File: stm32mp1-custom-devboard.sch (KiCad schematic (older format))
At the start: 0 parts

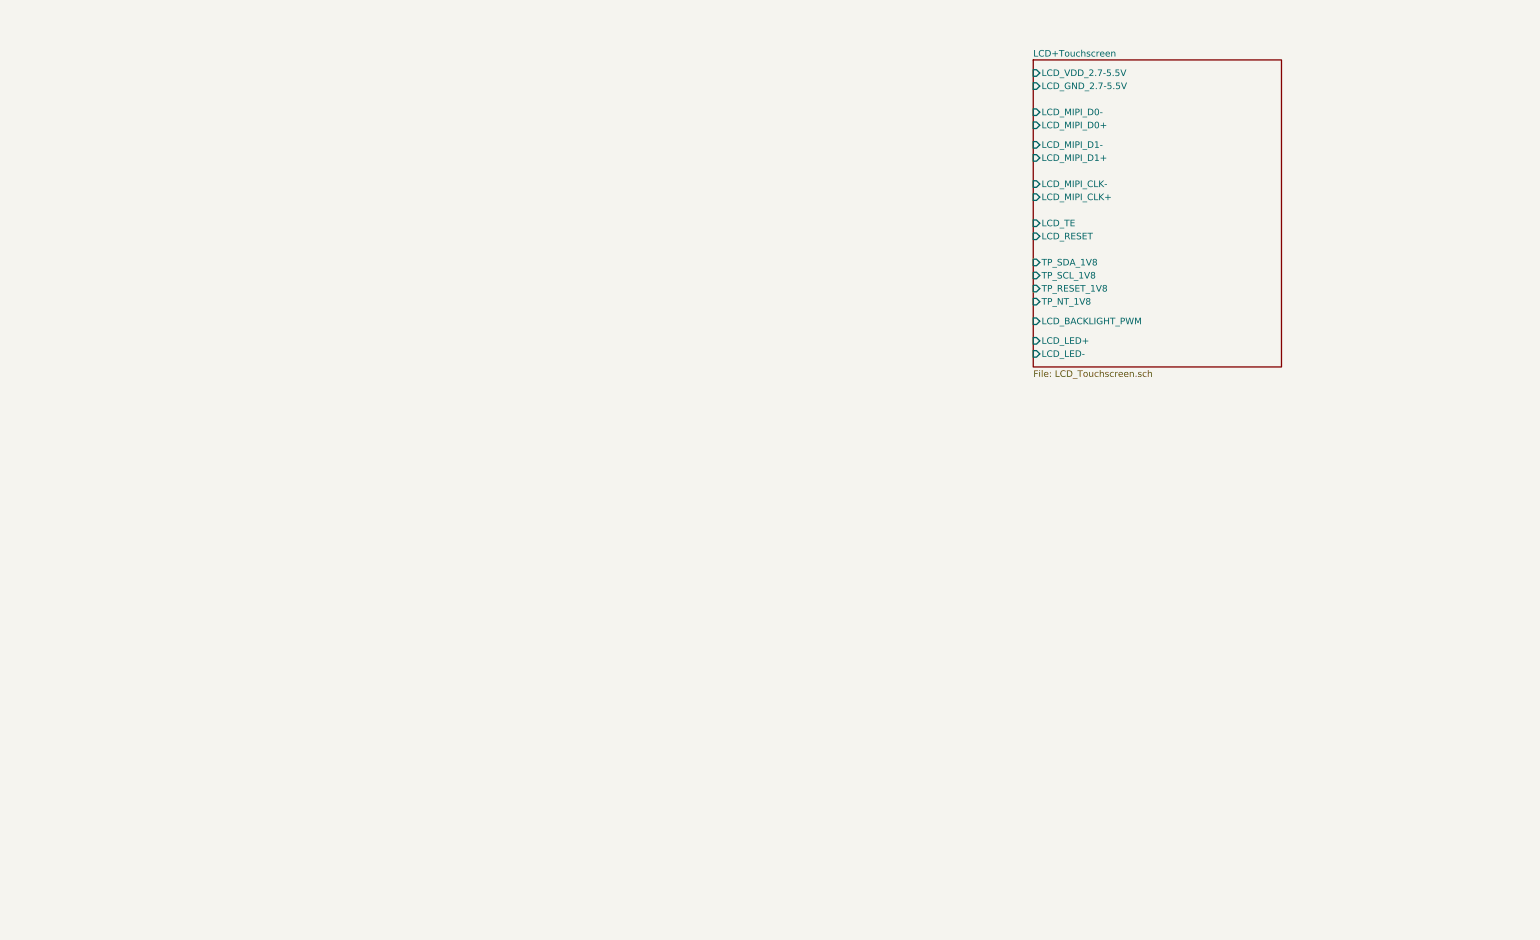
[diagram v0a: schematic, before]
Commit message: Added stm32mp1 module and arduino shield
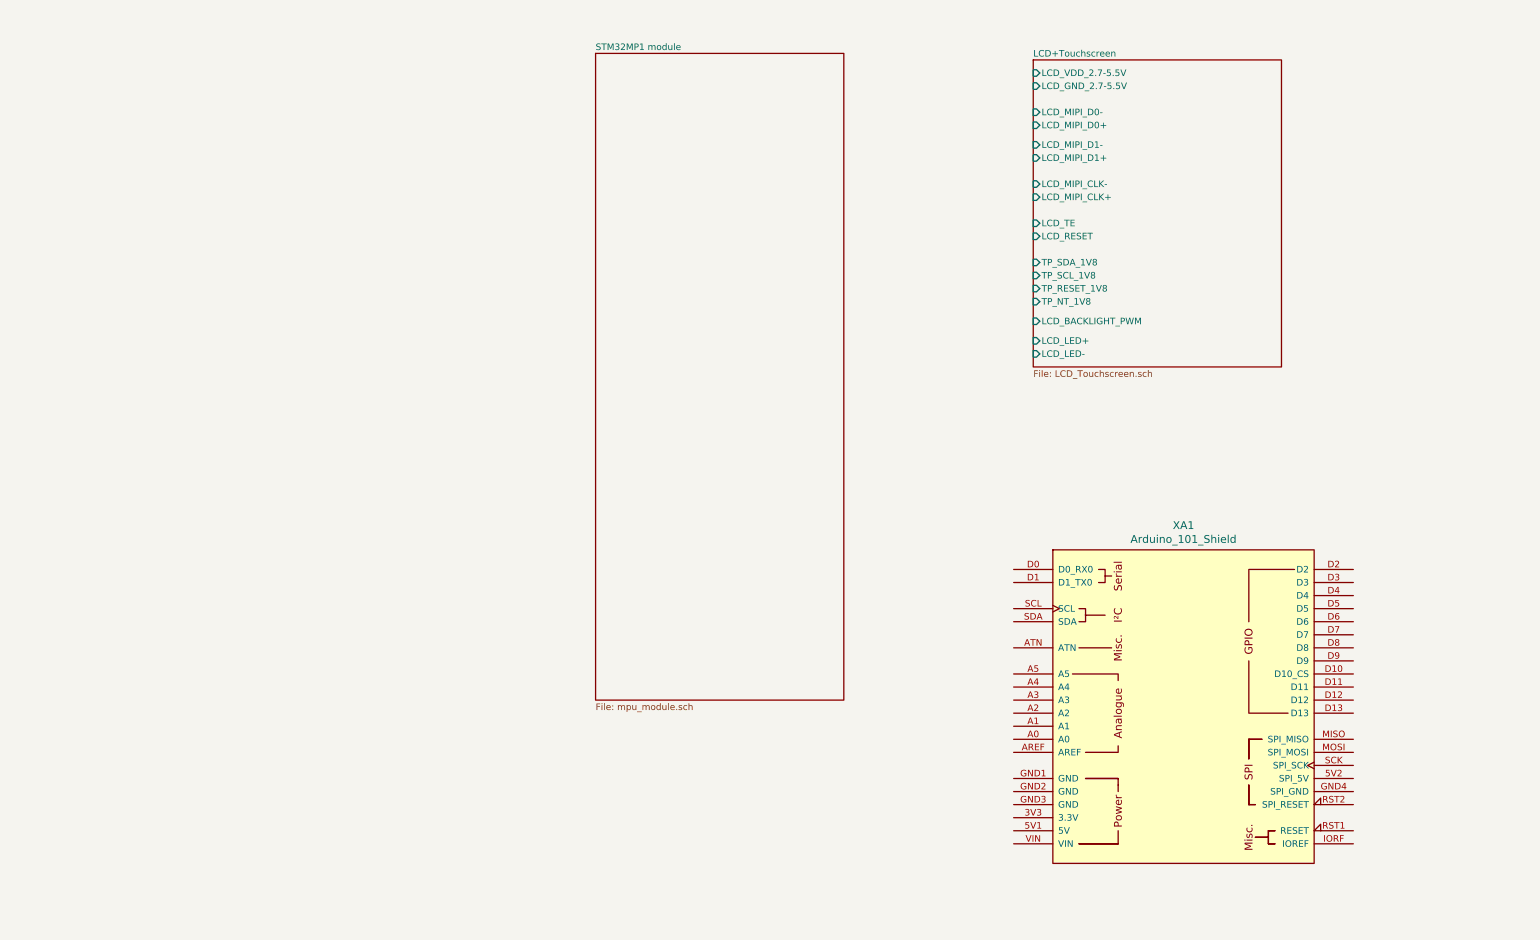
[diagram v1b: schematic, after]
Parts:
- added XA1: Arduino_101_Shield, Arduino:Arduino_101_Shield, symbol arduino:Arduino_101_Shield
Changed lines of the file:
@@
 $Descr A3 16535 11693
 encoding utf-8
-Sheet 1 4
+Sheet 1 5
 Title "stm32mp1-custom-devboard"
 Date "2020-12-19"
@@
 F18 "LCD_LED-" I L 10800 3900 50
 $EndSheet
+$Sheet
+S 7450 1600 1900 4950
+U 5FDE4F7C
+F0 "STM32MP1 module" 50
+F1 "mpu_module.sch" 50
+$EndSheet
+$Comp
+L arduino:Arduino_101_Shield XA1
+U 1 1 5FEBC8FE
+P 11950 6600
+F 0 "XA1" H 11950 7987 60  0000 C CNN
+F 1 "Arduino_101_Shield" H 11950 7881 60  0000 C CNN
+F 2 "Arduino:Arduino_101_Shield" H 13750 10350 60  0001 C CNN
+F 3 "" H 13750 10350 60  0001 C CNN
+	1    11950 6600
+	1    0    0    -1
+$EndComp
 $EndSCHEMATC

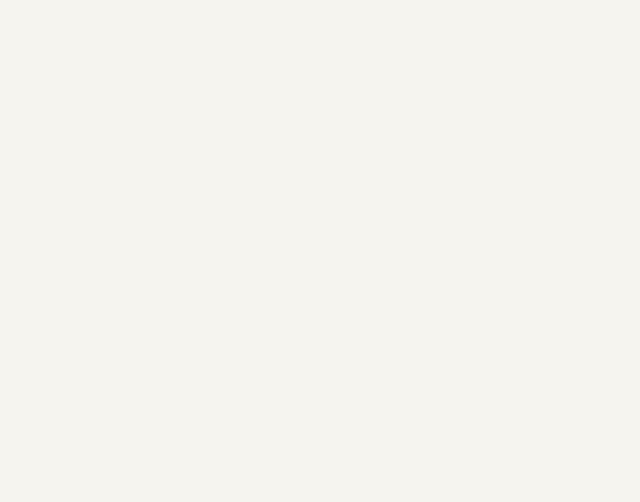
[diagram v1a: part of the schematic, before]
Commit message: Added new components and hierarchical sheets
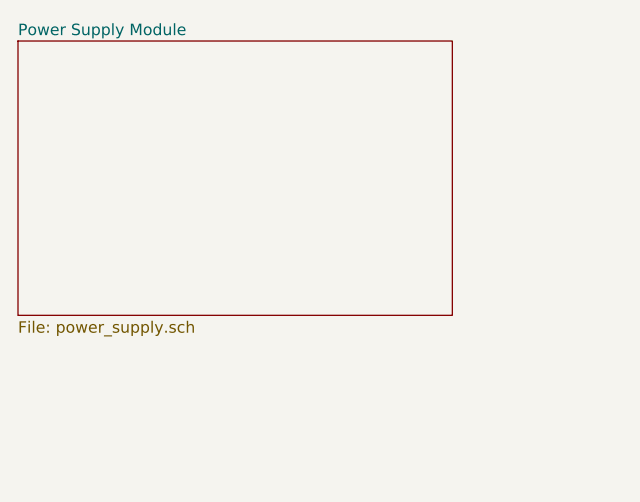
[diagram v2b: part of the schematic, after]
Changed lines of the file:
@@
 $Descr A3 16535 11693
 encoding utf-8
-Sheet 1 5
+Sheet 1 6
 Title "stm32mp1-custom-devboard"
 Date "2020-12-19"
@@
 	1    0    0    -1
 $EndComp
+$Sheet
+S 4400 1600 1900 1200
+U 5FDE84C9
+F0 "Power Supply Module" 50
+F1 "power_supply.sch" 50
+$EndSheet
 $EndSCHEMATC

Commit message: Added power source module
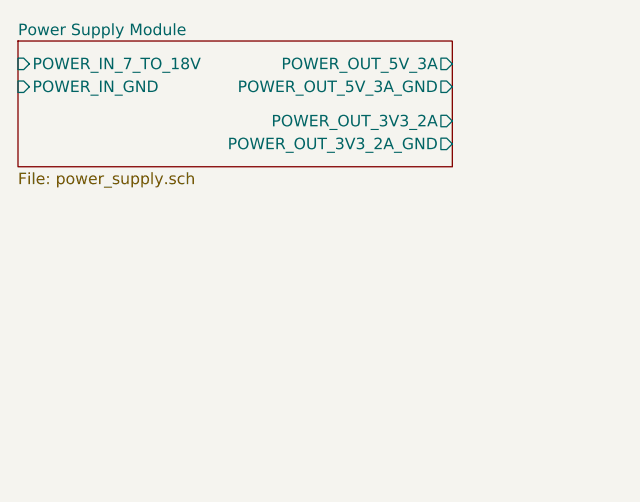
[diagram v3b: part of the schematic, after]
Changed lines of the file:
@@
 $EndComp
 $Sheet
-S 4400 1600 1900 1200
+S 4400 1600 1900 550
 U 5FDE84C9
 F0 "Power Supply Module" 50
 F1 "power_supply.sch" 50
+F2 "POWER_IN_7_TO_18V" I L 4400 1700 50
+F3 "POWER_IN_GND" I L 4400 1800 50
+F4 "POWER_OUT_5V_3A" O R 6300 1700 50
+F5 "POWER_OUT_5V_3A_GND" O R 6300 1800 50
+F6 "POWER_OUT_3V3_2A" O R 6300 1950 50
+F7 "POWER_OUT_3V3_2A_GND" O R 6300 2050 50
 $EndSheet
 $EndSCHEMATC

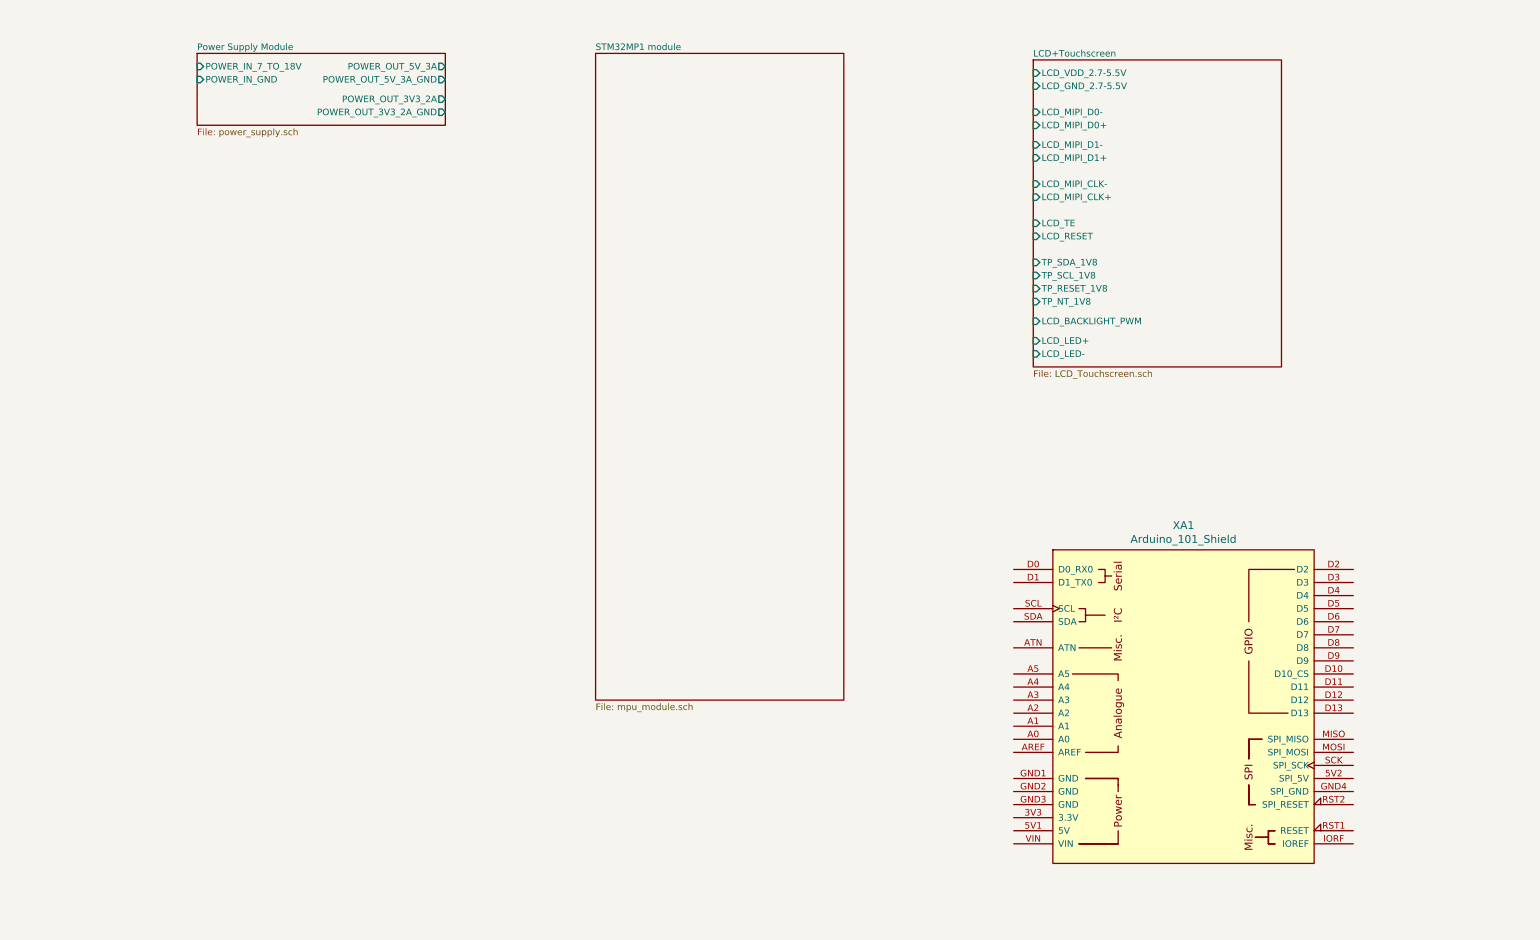
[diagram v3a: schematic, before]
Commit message: Added Mipi Dsi connection, started stlink module
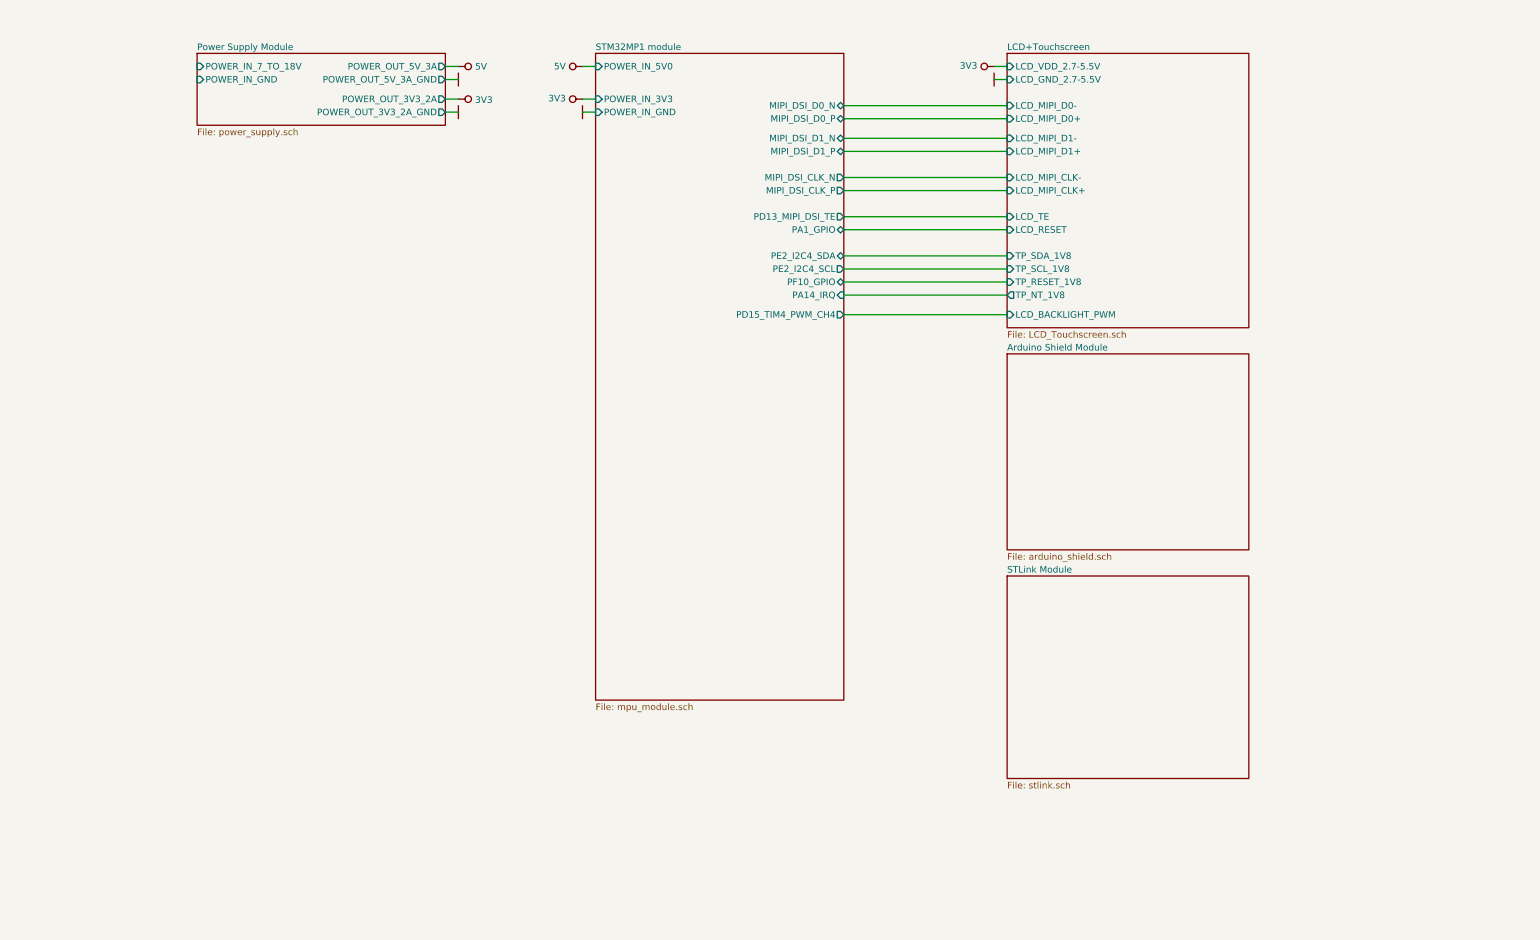
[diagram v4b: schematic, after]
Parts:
- removed XA1: Arduino_101_Shield, Arduino:Arduino_101_Shield, symbol arduino:Arduino_101_Shield
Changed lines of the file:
@@
 $Descr A3 16535 11693
 encoding utf-8
-Sheet 1 6
+Sheet 1 8
 Title "stm32mp1-custom-devboard"
 Date "2020-12-19"
@@
 $EndDescr
 $Sheet
-S 10800 1650 1900 2350
+S 10600 1600 1850 2100
 U 5EA691F1
 F0 "LCD+Touchscreen" 50
 F1 "LCD_Touchscreen.sch" 50
-F2 "LCD_MIPI_D1-" I L 10800 2300 50
-F3 "LCD_MIPI_D1+" I L 10800 2400 50
-F4 "LCD_MIPI_D0-" I L 10800 2050 50
-F5 "LCD_MIPI_D0+" I L 10800 2150 50
-F6 "LCD_MIPI_CLK-" I L 10800 2600 50
-F7 "LCD_MIPI_CLK+" I L 10800 2700 50
-F8 "LCD_BACKLIGHT_PWM" I L 10800 3650 50
-F9 "LCD_VDD_2.7-5.5V" I L 10800 1750 50
-F10 "TP_SDA_1V8" I L 10800 3200 50
-F11 "TP_SCL_1V8" I L 10800 3300 50
-F12 "TP_RESET_1V8" I L 10800 3400 50
-F13 "TP_NT_1V8" I L 10800 3500 50
-F14 "LCD_RESET" I L 10800 3000 50
-F15 "LCD_TE" I L 10800 2900 50
-F16 "LCD_GND_2.7-5.5V" I L 10800 1850 50
-F17 "LCD_LED+" I L 10800 3800 50
-F18 "LCD_LED-" I L 10800 3900 50
+F2 "LCD_MIPI_D1-" I L 10600 2250 50
+F3 "LCD_MIPI_D1+" I L 10600 2350 50
+F4 "LCD_MIPI_D0-" I L 10600 2000 50
+F5 "LCD_MIPI_D0+" I L 10600 2100 50
+F6 "LCD_MIPI_CLK-" I L 10600 2550 50
+F7 "LCD_MIPI_CLK+" I L 10600 2650 50
+F8 "LCD_BACKLIGHT_PWM" I L 10600 3600 50
+F9 "LCD_VDD_2.7-5.5V" I L 10600 1700 50
+F10 "TP_SDA_1V8" I L 10600 3150 50
+F11 "TP_SCL_1V8" I L 10600 3250 50
+F12 "TP_RESET_1V8" I L 10600 3350 50
+F13 "LCD_RESET" I L 10600 2950 50
+F14 "LCD_TE" I L 10600 2850 50
+F15 "LCD_GND_2.7-5.5V" I L 10600 1800 50
+F16 "TP_NT_1V8" O L 10600 3450 50
 $EndSheet
 $Sheet
@@
 F0 "STM32MP1 module" 50
 F1 "mpu_module.sch" 50
-$EndSheet
-$Comp
-L arduino:Arduino_101_Shield XA1
-U 1 1 5FEBC8FE
-P 11950 6600
-F 0 "XA1" H 11950 7987 60  0000 C CNN
-F 1 "Arduino_101_Shield" H 11950 7881 60  0000 C CNN
-F 2 "Arduino:Arduino_101_Shield" H 13750 10350 60  0001 C CNN
-F 3 "" H 13750 10350 60  0001 C CNN
-	1    11950 6600
-	1    0    0    -1
-$EndComp
+F2 "MIPI_DSI_CLK_P" O R 9350 2650 50
+F3 "MIPI_DSI_CLK_N" O R 9350 2550 50
+F4 "MIPI_DSI_D1_P" B R 9350 2350 50
+F5 "MIPI_DSI_D1_N" B R 9350 2250 50
+F6 "MIPI_DSI_D0_P" B R 9350 2100 50
+F7 "MIPI_DSI_D0_N" B R 9350 2000 50
+F8 "POWER_IN_5V0" I L 7450 1700 50
+F9 "POWER_IN_3V3" I L 7450 1950 50
+F10 "POWER_IN_GND" I L 7450 2050 50
+F11 "PE2_I2C4_SCL" O R 9350 3250 50
+F12 "PE2_I2C4_SDA" B R 9350 3150 50
+F13 "PD15_TIM4_PWM_CH4" O R 9350 3600 50
+F14 "PA14_IRQ" I R 9350 3450 50
+F15 "PA1_GPIO" B R 9350 2950 50
+F16 "PF10_GPIO" B R 9350 3350 50
+F17 "PD13_MIPI_DSI_TE" O R 9350 2850 50
+$EndSheet
 $Sheet
 S 4400 1600 1900 550
@@
 F7 "POWER_OUT_3V3_2A_GND" O R 6300 2050 50
 $EndSheet
+$Comp
+L power:5V #PWR0101
+U 1 1 5FDFA2F4
+P 6400 1700
+F 0 "#PWR0101" V 6350 1700 20  0001 C CNN
+F 1 "5V" V 6401 1828 50  0000 L CNN
+F 2 "" H 6400 1700 60  0000 C CNN
+F 3 "" H 6400 1700 60  0000 C CNN
+	1    6400 1700
+	0    1    1    0
+$EndComp
+$Comp
+L power:GND #PWR0109
+U 1 1 5FDFAC1E
+P 6400 1800
+F 0 "#PWR0109" H 6400 1900 30  0001 C CNN
+F 1 "GND" H 6400 1700 30  0001 C CNN
+F 2 "" H 6400 1800 60  0000 C CNN
+F 3 "" H 6400 1800 60  0000 C CNN
+	1    6400 1800
+	0    1    1    0
+$EndComp
+$Comp
+L power:GND #PWR0110
+U 1 1 5FDFB10E
+P 6400 2050
+F 0 "#PWR0110" H 6400 2150 30  0001 C CNN
+F 1 "GND" H 6400 1950 30  0001 C CNN
+F 2 "" H 6400 2050 60  0000 C CNN
+F 3 "" H 6400 2050 60  0000 C CNN
+	1    6400 2050
+	0    1    1    0
+$EndComp
+$Comp
+L power:3V3 #PWR0111
+U 1 1 5FDFB5C2
+P 6400 1950
+F 0 "#PWR0111" H 6400 2050 40  0001 C CNN
+F 1 "3V3" V 6406 2078 50  0000 L CNN
+F 2 "" H 6400 1950 60  0000 C CNN
+F 3 "" H 6400 1950 60  0000 C CNN
+	1    6400 1950
+	0    1    1    0
+$EndComp
+Wire Wire Line
+	6400 1700 6300 1700
+Wire Wire Line
+	6300 1800 6400 1800
+Wire Wire Line
+	6400 1950 6300 1950
+Wire Wire Line
+	6300 2050 6400 2050
+$Comp
+L power:GND #PWR0112
+U 1 1 5FDFCB8E
+P 10500 1800
+F 0 "#PWR0112" H 10500 1900 30  0001 C CNN
+F 1 "GND" H 10500 1700 30  0001 C CNN
+F 2 "" H 10500 1800 60  0000 C CNN
+F 3 "" H 10500 1800 60  0000 C CNN
+	1    10500 1800
+	0    -1   -1   0
+$EndComp
+Wire Wire Line
+	10500 1700 10600 1700
+Wire Wire Line
+	10600 1800 10500 1800
+$Comp
+L power:3V3 #PWR0113
+U 1 1 5FDFE1EC
+P 10500 1700
+F 0 "#PWR0113" H 10500 1800 40  0001 C CNN
+F 1 "3V3" V 10506 1828 50  0000 L CNN
+F 2 "" H 10500 1700 60  0000 C CNN
+F 3 "" H 10500 1700 60  0000 C CNN
+	1    10500 1700
+	0    -1   -1   0
+$EndComp
+Wire Wire Line
+	10600 2000 9350 2000
+Wire Wire Line
+	10600 2100 9350 2100
+Wire Wire Line
+	10600 2250 9350 2250
+Wire Wire Line
+	10600 2350 9350 2350
+Wire Wire Line
+	10600 2550 9350 2550
+Wire Wire Line
+	10600 2650 9350 2650
+Wire Wire Line
+	10600 2850 9350 2850
+Wire Wire Line
+	10600 2950 9350 2950
+Wire Wire Line
+	10600 3150 9350 3150
+Wire Wire Line
+	10600 3250 9350 3250
+Wire Wire Line
+	10600 3350 9350 3350
+Wire Wire Line
+	10600 3450 9350 3450
+Wire Wire Line
+	10600 3600 9350 3600
+$Comp
+L power:5V #PWR0114
+U 1 1 5FFE2EA9
+P 7350 1700
+F 0 "#PWR0114" V 7300 1700 20  0001 C CNN
+F 1 "5V" V 7351 1828 50  0000 L CNN
+F 2 "" H 7350 1700 60  0000 C CNN
+F 3 "" H 7350 1700 60  0000 C CNN
+	1    7350 1700
+	0    -1   -1   0
+$EndComp
+$Comp
+L power:GND #PWR0115
+U 1 1 5FFE3C7C
+P 7350 2050
+F 0 "#PWR0115" H 7350 2150 30  0001 C CNN
+F 1 "GND" H 7350 1950 30  0001 C CNN
+F 2 "" H 7350 2050 60  0000 C CNN
+F 3 "" H 7350 2050 60  0000 C CNN
+	1    7350 2050
+	0    -1   -1   0
+$EndComp
+Wire Wire Line
+	7450 2050 7350 2050
+$Comp
+L power:3V3 #PWR0116
+U 1 1 5FFE4439
+P 7350 1950
+F 0 "#PWR0116" H 7350 2050 40  0001 C CNN
+F 1 "3V3" V 7356 2078 50  0000 L CNN
+F 2 "" H 7350 1950 60  0000 C CNN
+F 3 "" H 7350 1950 60  0000 C CNN
+	1    7350 1950
+	0    -1   -1   0
+$EndComp
+Wire Wire Line
+	7350 1950 7450 1950
+Wire Wire Line
+	7450 1700 7350 1700
+$Sheet
+S 10600 3900 1850 1500
+U 60087A46
+F0 "Arduino Shield Module" 50
+F1 "arduino_shield.sch" 50
+$EndSheet
+$Sheet
+S 10600 5600 1850 1550
+U 5FDFB166
+F0 "STLink Module" 50
+F1 "stlink.sch" 50
+$EndSheet
 $EndSCHEMATC

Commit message: Added minipci connector
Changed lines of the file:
@@
 $Descr A3 16535 11693
 encoding utf-8
-Sheet 1 8
+Sheet 1 9
 Title "stm32mp1-custom-devboard"
 Date "2020-12-19"
@@
 F1 "stlink.sch" 50
 $EndSheet
+$Sheet
+S 12750 3900 1850 1500
+U 5FFEC95A
+F0 "MiniPci Module" 50
+F1 "minipci_module.sch" 50
+$EndSheet
 $EndSCHEMATC
